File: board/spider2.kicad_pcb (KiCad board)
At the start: 2 copper layers, 137 x 75.5 mm, 136 parts, among them J1 NRJ6HH-1, J10 PJ-320A, J11 PJ358, J12 PJ358, J13 PJ358, J14 PJ358, J15 PJ358, J16 PJ358, J19 PJ358, J2 NRJ6HH-1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

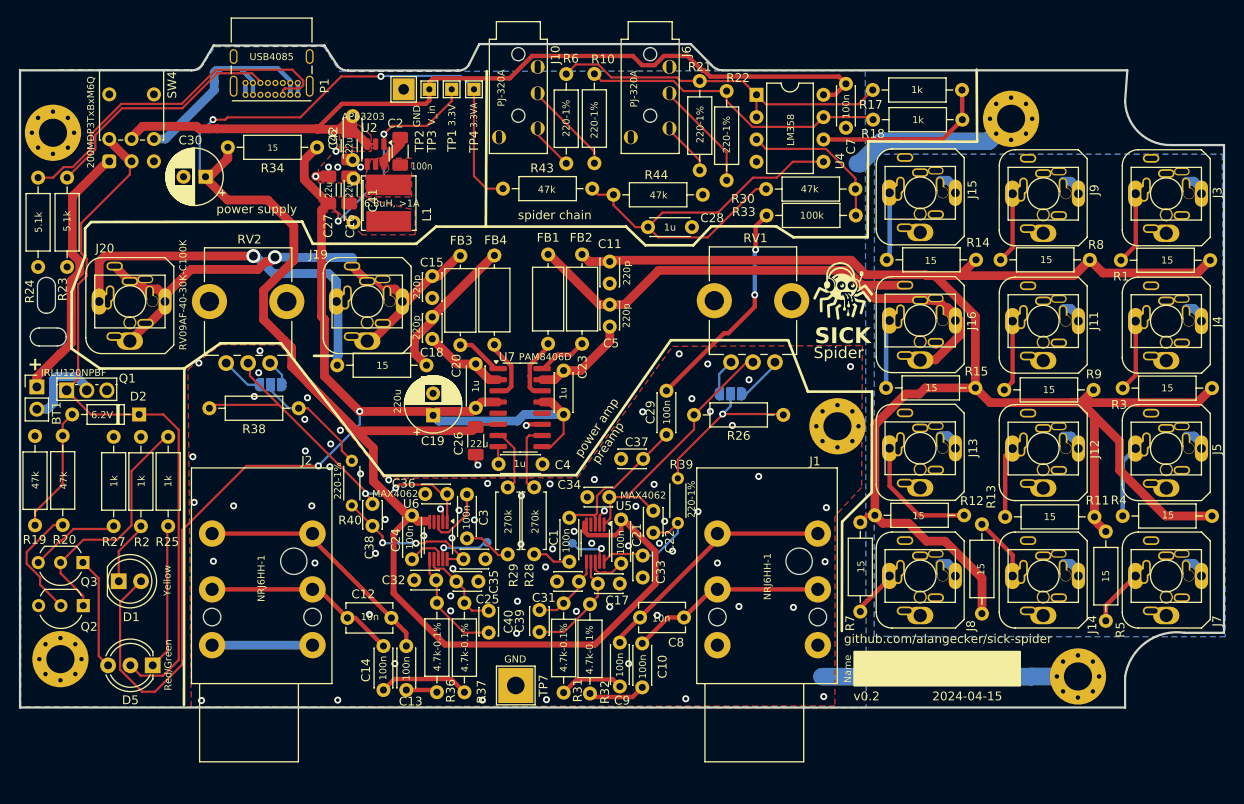
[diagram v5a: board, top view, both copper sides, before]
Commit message: redesigned MAX section with shorter traces, analog GND plane,...
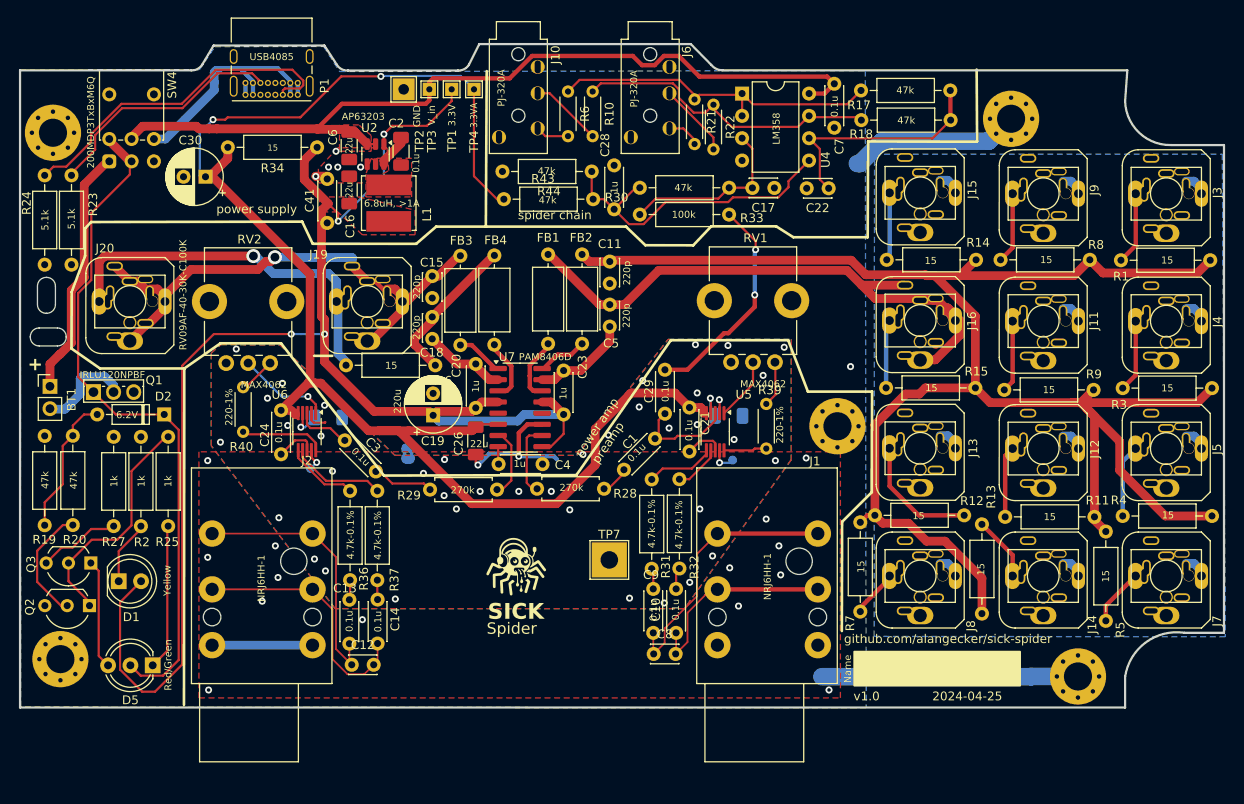
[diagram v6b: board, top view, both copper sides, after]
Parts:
- removed C25, C31, C32, C33, C34, C35, C36, C37, C38, C39, C40: 220p, Capacitor_THT:C_Disc_D3.0mm_W2.0mm_P2.50mm
- removed JP2: ~, Jumper:SolderJumper-3_P1.3mm_Open_RoundedPad1.0x1.5mm_NumberLabels
- removed R26, R38: dnp, Resistor_THT:R_Axial_DIN0207_L6.3mm_D2.5mm_P10.16mm_Horizontal
- C1, C10, C13, C14, C2, C21, C24, C29, C3, C7, C9: value 100n -> 0.1u
- C12, C8: value 10n -> 220p; footprint Capacitor_THT:C_Disc_D5.1mm_W3.2mm_P5.00mm -> Capacitor_THT:C_Disc_D3.0mm_W2.0mm_P2.50mm
- C27: value 22u -> dnp; moved to B.Cu
- C42: footprint Capacitor_THT:C_Disc_D4.3mm_W1.9mm_P5.00mm -> Capacitor_SMD:C_1206_3216Metric_Pad1.33x1.80mm_HandSolder; moved to B.Cu
- JP1: footprint Jumper:SolderJumper-3_P1.3mm_Open_RoundedPad1.0x1.5mm_NumberLabels -> Jumper:SolderJumper-2_P1.3mm_Bridged2Bar_RoundedPad1.0x1.5mm
- R10, R21, R22, R6: footprint Resistor_THT:R_Axial_DIN0207_L6.3mm_D2.5mm_P10.16mm_Horizontal -> Resistor_THT:R_Axial_DIN0204_L3.6mm_D1.6mm_P5.08mm_Horizontal
- R17, R18: value 1k -> 47k
- TP7: value GND -> GNDA
- moved C27 52.3 mm to (218.3, 69.9), turned to 180 degrees
- moved C17 49.3 mm to (223.5, 44.0), turned to 180 degrees
- moved C22 41.8 mm to (229.7, 44.0), turned to 180 degrees
- moved JP1 37.3 mm to (181.8, 74.2), turned to -90 degrees
- moved C42 29.4 mm to (172.7, 70.1), turned to 180 degrees
- moved R33 24.6 mm to (208.2, 47.0), turned to 0 degrees
- moved TP6 21.8 mm to (170.7, 75.9)
- moved TP5 20.5 mm to (218.7, 74.9)
- moved U6 19.4 mm to (170.3, 71.7)
- moved C24 19.1 mm to (167.3, 69.3)
- moved U5 18.6 mm to (216.8, 71.7)
- moved TP7 17.8 mm to (204.7, 86.3)
- moved R32 17.5 mm to (212.7, 87.3)
- moved R31 17.3 mm to (209.5, 87.3)
- moved R37 16.2 mm to (178.3, 88.6)
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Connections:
- net Net-(U4B-+) renamed /CMV
- C17 pad 1: Net-(U5-IN-) -> GND
- C17 pad 2: GND -> Net-(U4A-+)
- C21 pad 2: GND -> GNDA
- C22 pad 1: Net-(U5-G2) -> Net-(U4B--)
- C22 pad 2: Net-(U5-G1) -> GND
- C24 pad 2: GND -> GNDA
- C26 pad 2: GND -> GNDA
- C27 pad 1: GND -> GNDA
- C27 pad 2: +3.3V -> Net-(U5-BIAS)
- C4 pad 1: GND -> GNDA
- C42 pad 1: GND -> GNDA
- C42 pad 2: VCC -> Net-(U6-BIAS)
- JP1 pad 1: Net-(JP1-A) -> GND
- JP1 pad 2: Net-(JP1-C) -> GNDA
- R39 pad 2: Net-(JP1-C) -> Net-(R39-Pad2)
- R40 pad 2: Net-(JP2-C) -> Net-(R40-Pad2)
- RV1 pad 1: Net-(JP1-A) -> Net-(R39-Pad2)
- RV1 pad 3: Net-(JP1-B) -> unconnected-(RV1-Pad3)
- RV2 pad 1: Net-(JP2-A) -> Net-(R40-Pad2)
- RV2 pad 3: Net-(JP2-B) -> unconnected-(RV2-Pad3)
- TP7 pad 1: GND -> GNDA
- U5 pad 2: GND -> GNDA
- U5 pad 4: unconnected-(U5-BIAS-Pad4) -> Net-(U5-BIAS)
- U5 pad 8: GND -> GNDA
- U6 pad 2: GND -> GNDA
- U6 pad 4: unconnected-(U6-BIAS-Pad4) -> Net-(U6-BIAS)
- U6 pad 8: GND -> GNDA
- U7 pad 11: GND -> GNDA
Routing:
- net Net-(U6-G2): track 42.9 -> 10.6 mm, vias 2 -> 1
- net +3.3VA: track 199.6 -> 167.8 mm
- net GNDA: track 0.00 -> 29.9 mm, vias 0 -> 41
- net Net-(U5-G2): track 31.2 -> 7.17 mm
- net Net-(JP1-C): track 19.0 -> 0.00 mm, vias 1 -> 0
- net GND: track 100.9 -> 85.1 mm, vias 80 -> 20
- net Net-(JP2-C): track 13.8 -> 0.00 mm
- net /CMV: track 48.1 -> 36.3 mm
- net Net-(U5-G1): track 14.3 -> 4.89 mm
- net +3.3V: track 163.0 -> 171.8 mm
- net Net-(C14-Pad2): track 10.4 -> 2.22 mm
- net Net-(U6-G1): track 17.7 -> 9.62 mm, vias 2 -> 0
- net Net-(U5-IN-): track 12.7 -> 5.42 mm
- net Net-(U4B--): track 20.1 -> 27.0 mm
- net /Preamp Floor/IN-: track 22.2 -> 28.8 mm
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- added copper zone on B.Cu, net GNDA
- added copper zone on F.Cu, net GNDA
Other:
- board text added: "2024-04-25"
- board text added: "v1.0"
- board text removed: "2024-04-15"
- board text removed: "v0.2"

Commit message: revert separating ground planes
maybe it leads to more issues than it solves
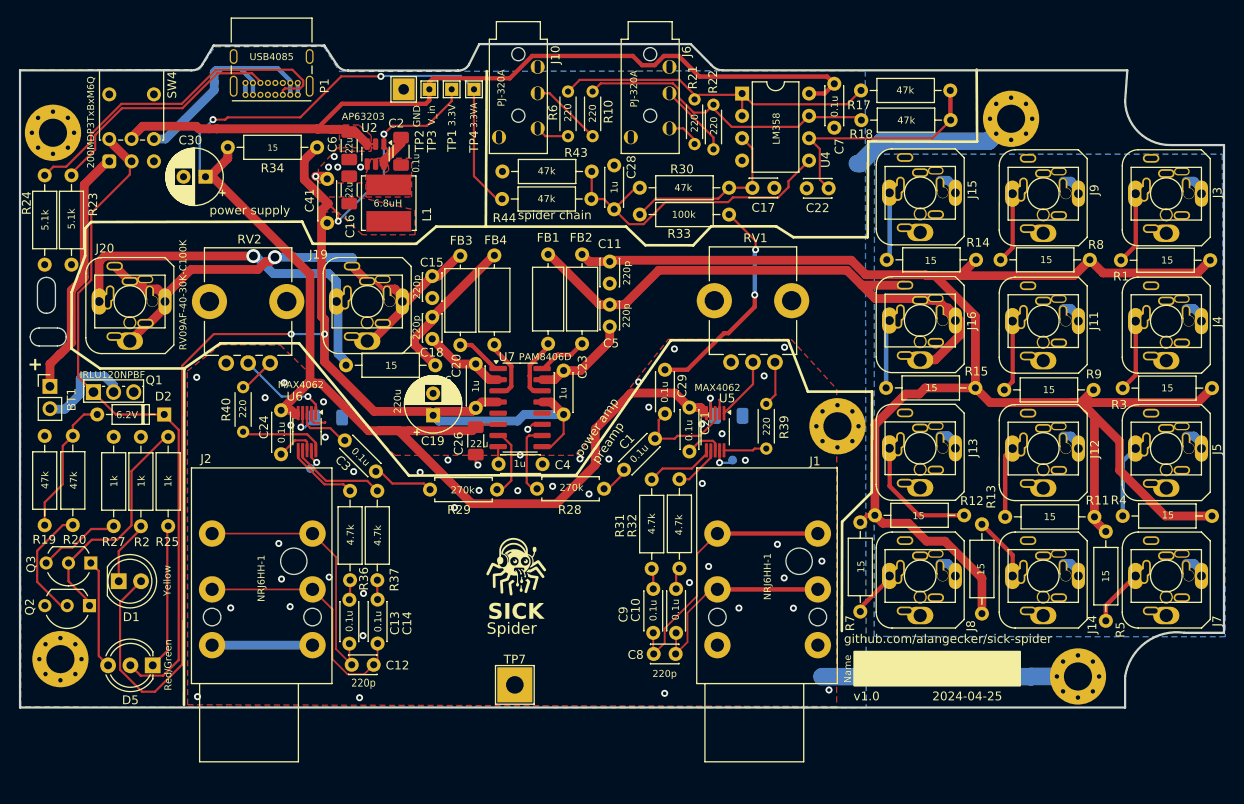
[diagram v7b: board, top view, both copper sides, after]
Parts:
- removed JP1: ~, Jumper:SolderJumper-2_P1.3mm_Bridged2Bar_RoundedPad1.0x1.5mm
- FB1: value 3A, >100 Ohm@100MHz -> 3A/≥100 Ohm
- L1: value 6.8uH, >1A -> 6.8uH
- R10, R21, R22, R39, R40, R6: value 220-1% -> 220
- R31, R32, R36, R37: value 4.7k-0.1% -> 4.7k
- TP7: value GNDA -> GND
- moved TP7 17.8 mm to (193.9, 100.5)
- moved R43 0.20 mm to (192.5, 45.2)
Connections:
- C21 pad 2: GNDA -> GND
- C24 pad 2: GNDA -> GND
- C26 pad 2: GNDA -> GND
- C27 pad 1: GNDA -> GND
- C4 pad 1: GNDA -> GND
- C42 pad 1: GNDA -> GND
- TP7 pad 1: GNDA -> GND
- U5 pad 2: GNDA -> GND
- U5 pad 8: GNDA -> GND
- U6 pad 2: GNDA -> GND
- U6 pad 8: GNDA -> GND
- U7 pad 11: GNDA -> GND
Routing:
- net GNDA: track 29.9 -> 0.00 mm, vias 41 -> 0
- net GND: track 85.1 -> 101.3 mm, vias 20 -> 51
- removed copper zone on B.Cu, net GNDA
- removed copper zone on F.Cu, net GNDA
